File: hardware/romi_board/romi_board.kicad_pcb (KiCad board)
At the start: 2 copper layers, 99.1 x 66 mm, 33 parts, among them J1 Conn_01x14, J2 Conn_01x14, J3 Conn_01x04, SW1 SW_SPST, U1 Teensy4.0

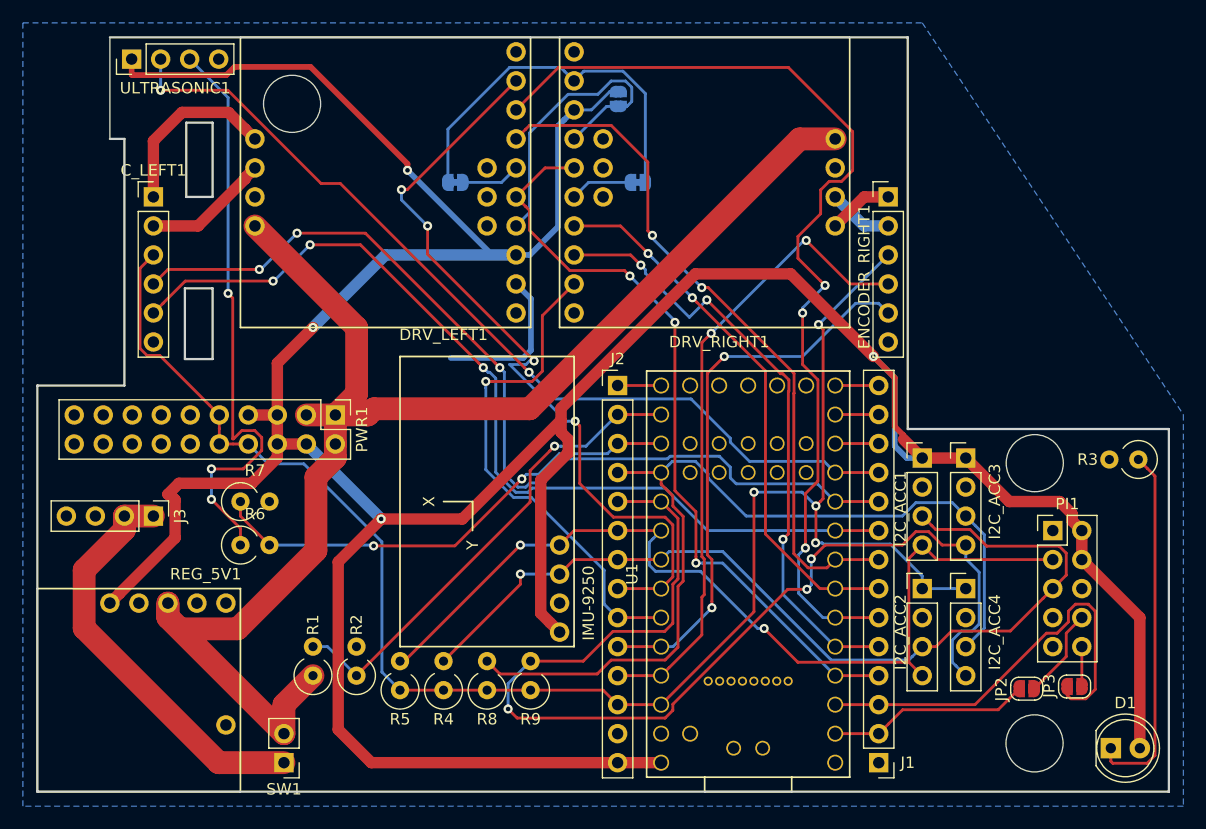
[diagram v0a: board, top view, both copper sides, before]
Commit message: flip the left motor encorder connector the right way round.
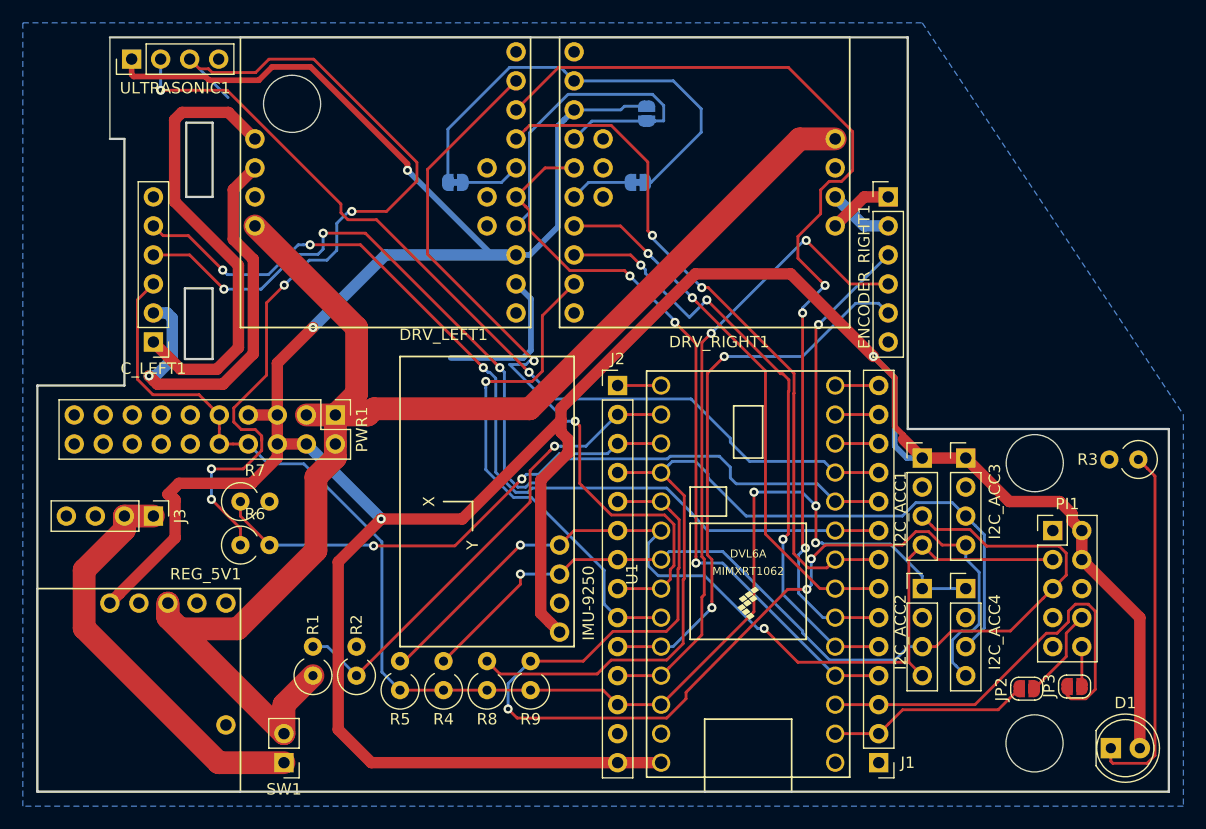
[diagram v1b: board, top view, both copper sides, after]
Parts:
- U1: footprint teensy:Teensy40_SMT -> teensy:Teensy40_simple
- moved C_LEFT1 12.7 mm to (69.2, 114.0), turned to 180 degrees
- moved JP1 2.79 mm to (112.4, 94.0)
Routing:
- net /US_ECHO_5V: track 51.8 -> 78.8 mm, vias 3 -> 4
- net /LM2: track 11.1 -> 36.4 mm, vias 0 -> 1
- net /LM1: track 15.8 -> 39.8 mm
- net GND: track 47.3 -> 53.0 mm
- net /XD_OCC: track 27.3 -> 32.0 mm
- net +5V: track 318.9 -> 321.2 mm
- net /LENCA: track 83.1 -> 85.3 mm
- net /LD_OCM: track 68.9 -> 66.9 mm, vias 4 -> 2
- net +3V3: track 146.9 -> 145.9 mm
- net /LD_PWM1: track 87.3 -> 86.4 mm
